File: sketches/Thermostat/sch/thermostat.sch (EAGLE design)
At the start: 11 parts, among them CN1 DHT22, CN2 OLED, SW1 BTN_UP, SW2 BTN_DOWN, SW3 BTN_CTRL, U1 MOTEINO

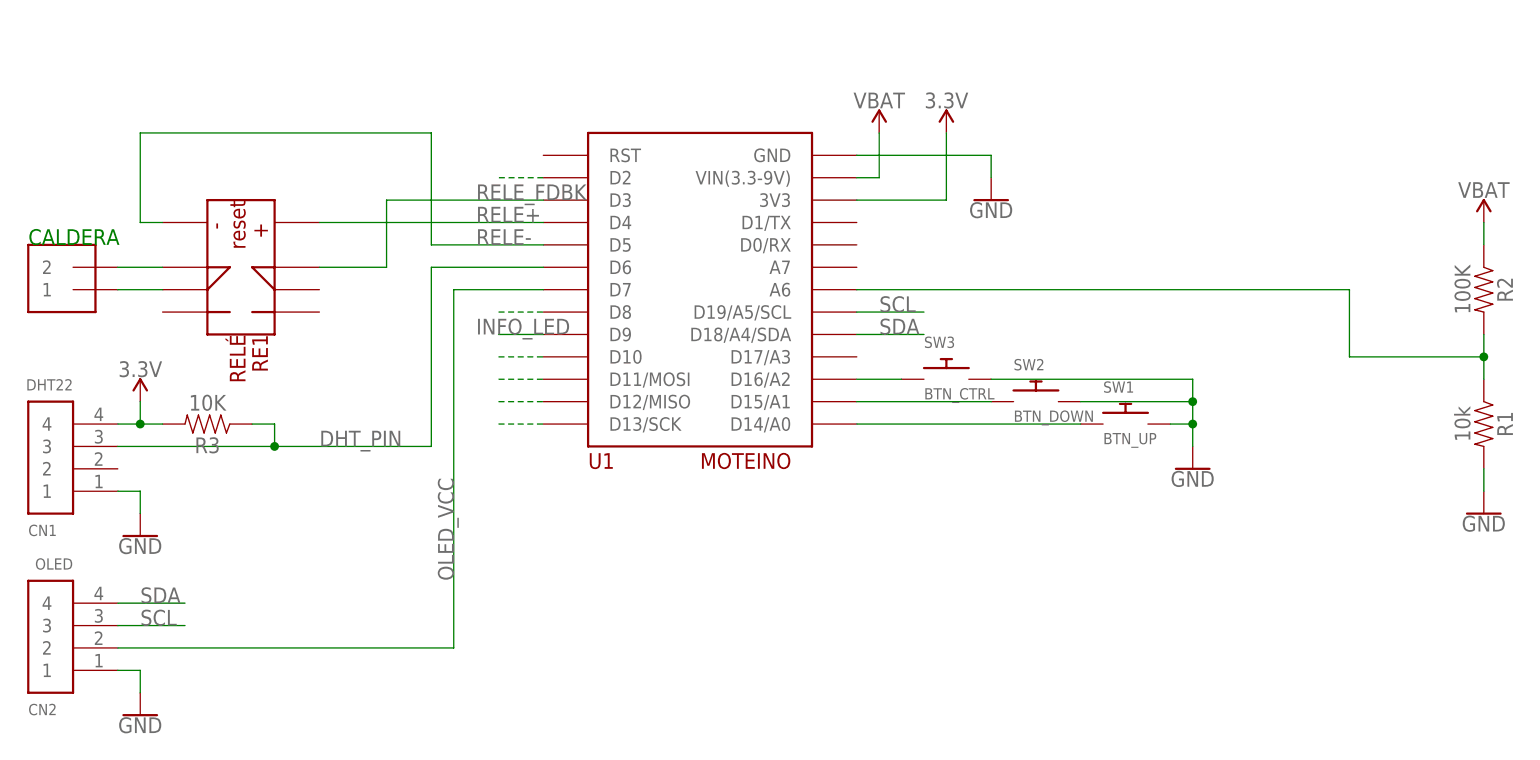
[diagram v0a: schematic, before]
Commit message: [Thermostat] Schematic updated as it is built in real life. v1
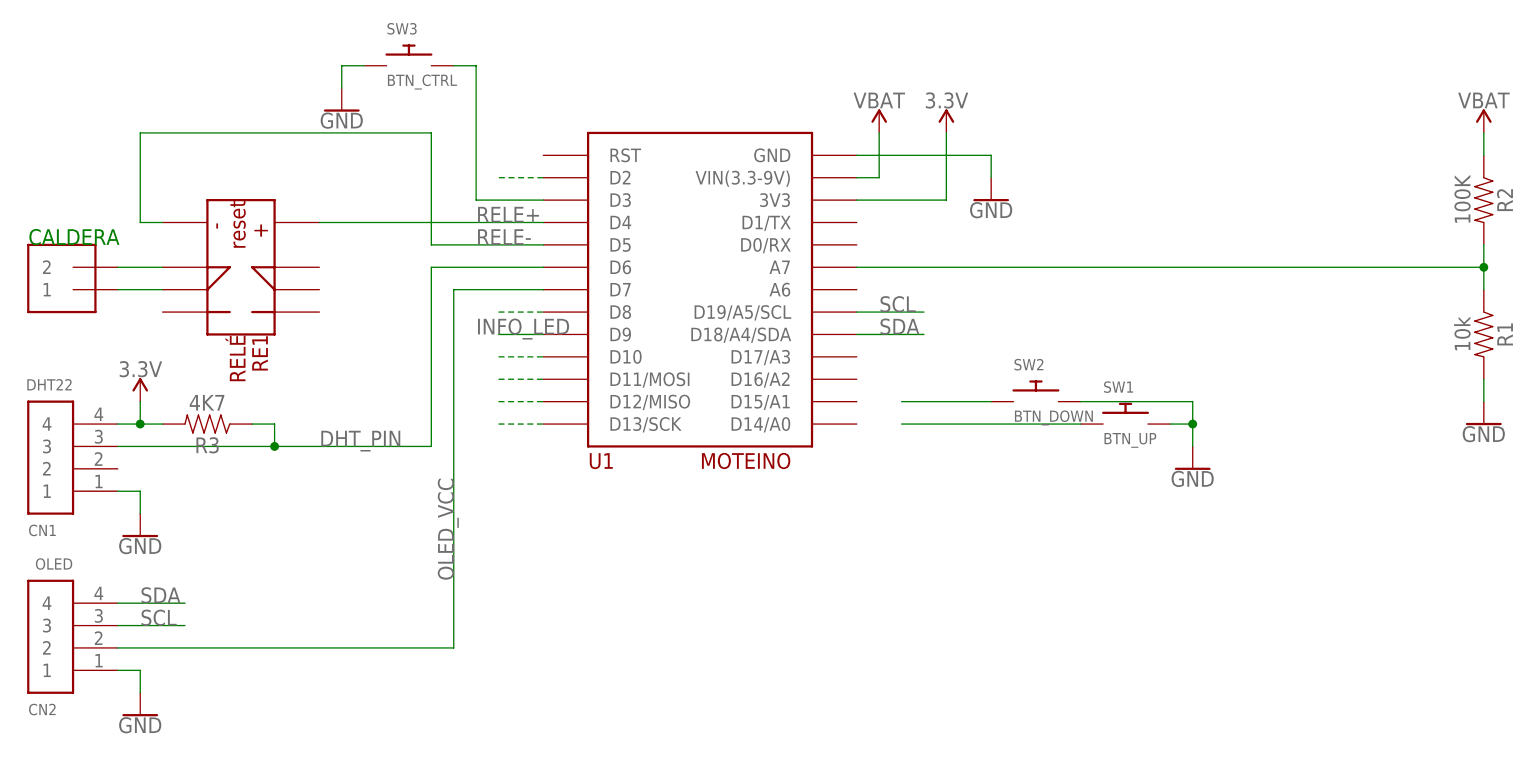
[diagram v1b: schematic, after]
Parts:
- R3: value 10K -> 4K7
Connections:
- removed net RELE_FDBK: RE1.P$8, U1.D3
- net GND: now also SW3.P$1; no longer SW3.P$2
- net N$1: now also SW3.P$2, U1.D3; no longer SW3.P$1, U1.D16/A2
- net N$3: now also U1.A7; no longer U1.A6
- net N$4: no longer U1.D15/A1
- net N$7: no longer U1.D14/A0
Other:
- moved on the sheet: R1, R2, SW3
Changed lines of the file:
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@@
 <part name="SW3" library="adafruit" deviceset="SWITCH_PUSHBUTTON" device="EVQ-PE" value="BTN_CTRL"/>
 <part name="GND6" library="SparkFun-PowerSymbols" deviceset="GND" device=""/>
-<part name="R3" library="SparkFun-Resistors" deviceset="RESISTOR" device="AXIAL-0.3" value="10K"/>
+<part name="R3" library="SparkFun-Resistors" deviceset="RESISTOR" device="AXIAL-0.3" value="4K7"/>
+<part name="GND2" library="SparkFun-PowerSymbols" deviceset="GND" device=""/>
 </parts>
 <sheets>
@@
 </plain>
 <instances>
-<instance part="R1" gate="G$1" x="132.08" y="7.62" rot="R270"/>
-<instance part="R2" gate="G$1" x="132.08" y="22.86" rot="R270"/>
-<instance part="GND1" gate="1" x="132.08" y="-2.54"/>
+<instance part="R1" gate="G$1" x="132.08" y="17.78" rot="R270"/>
+<instance part="R2" gate="G$1" x="132.08" y="33.02" rot="R270"/>
+<instance part="GND1" gate="1" x="132.08" y="7.62"/>
 <instance part="U1" gate="G$1" x="30.48" y="5.08"/>
 <instance part="SW2" gate="G$1" x="81.28" y="10.16"/>
@@
 <instance part="SUPPLY4" gate="G$1" x="63.5" y="40.64"/>
 <instance part="GND5" gate="1" x="76.2" y="33.02"/>
-<instance part="SUPPLY1" gate="G$1" x="132.08" y="30.48"/>
+<instance part="SUPPLY1" gate="G$1" x="132.08" y="40.64"/>
 <instance part="SW1" gate="G$1" x="91.44" y="7.62"/>
-<instance part="SW3" gate="G$1" x="71.12" y="12.7"/>
+<instance part="SW3" gate="G$1" x="10.16" y="48.26"/>
 <instance part="GND6" gate="1" x="99.06" y="2.54"/>
 <instance part="R3" gate="G$1" x="-12.7" y="7.62" rot="R180"/>
+<instance part="GND2" gate="1" x="2.54" y="43.18"/>
 </instances>
 <busses>
@@
 <segment>
 <pinref part="R1" gate="G$1" pin="2"/>
-<wire x1="132.08" y1="2.54" x2="132.08" y2="0" width="0.1524" layer="91"/>
+<wire x1="132.08" y1="12.7" x2="132.08" y2="10.16" width="0.1524" layer="91"/>
 <pinref part="GND1" gate="1" pin="GND"/>
 </segment>
@@
 </segment>
 <segment>
-<pinref part="SW3" gate="G$1" pin="P$2"/>
-<wire x1="76.2" y1="12.7" x2="99.06" y2="12.7" width="0.1524" layer="91"/>
-<wire x1="99.06" y1="12.7" x2="99.06" y2="10.16" width="0.1524" layer="91"/>
 <pinref part="SW2" gate="G$1" pin="P$2"/>
 <wire x1="99.06" y1="10.16" x2="99.06" y2="7.62" width="0.1524" layer="91"/>
 <wire x1="99.06" y1="7.62" x2="99.06" y2="5.08" width="0.1524" layer="91"/>
 <wire x1="86.36" y1="10.16" x2="99.06" y2="10.16" width="0.1524" layer="91"/>
-<junction x="99.06" y="10.16"/>
 <pinref part="SW1" gate="G$1" pin="P$2"/>
 <wire x1="96.52" y1="7.62" x2="99.06" y2="7.62" width="0.1524" layer="91"/>
@@
 <pinref part="GND6" gate="1" pin="GND"/>
 </segment>
+<segment>
+<pinref part="GND2" gate="1" pin="GND"/>
+<wire x1="2.54" y1="45.72" x2="2.54" y2="48.26" width="0.1524" layer="91"/>
+<pinref part="SW3" gate="G$1" pin="P$1"/>
+<wire x1="2.54" y1="48.26" x2="5.08" y2="48.26" width="0.1524" layer="91"/>
+</segment>
 </net>
 <net name="VCC" class="0">
@@
 <segment>
 <pinref part="R2" gate="G$1" pin="1"/>
-<wire x1="132.08" y1="27.94" x2="132.08" y2="30.48" width="0.1524" layer="91"/>
+<wire x1="132.08" y1="38.1" x2="132.08" y2="40.64" width="0.1524" layer="91"/>
 <pinref part="SUPPLY1" gate="G$1" pin="VCC"/>
 </segment>
@@
 <pinref part="R2" gate="G$1" pin="2"/>
 <pinref part="R1" gate="G$1" pin="1"/>
-<wire x1="132.08" y1="12.7" x2="132.08" y2="15.24" width="0.1524" layer="91"/>
-<pinref part="U1" gate="G$1" pin="A6"/>
-<wire x1="132.08" y1="15.24" x2="132.08" y2="17.78" width="0.1524" layer="91"/>
-<wire x1="60.96" y1="22.86" x2="116.84" y2="22.86" width="0.1524" layer="91"/>
-<wire x1="116.84" y1="22.86" x2="116.84" y2="15.24" width="0.1524" layer="91"/>
-<wire x1="116.84" y1="15.24" x2="132.08" y2="15.24" width="0.1524" layer="91"/>
-<junction x="132.08" y="15.24"/>
+<wire x1="132.08" y1="22.86" x2="132.08" y2="25.4" width="0.1524" layer="91"/>
+<wire x1="132.08" y1="25.4" x2="132.08" y2="27.94" width="0.1524" layer="91"/>
+<junction x="132.08" y="25.4"/>
+<pinref part="U1" gate="G$1" pin="A7"/>
+<wire x1="60.96" y1="25.4" x2="132.08" y2="25.4" width="0.1524" layer="91"/>
 </segment>
 </net>
@@
 </segment>
 </net>
-<net name="RELE_FDBK" class="0">
-<segment>
-<pinref part="RE1" gate="G$1" pin="P$8"/>
-<wire x1="0" y1="25.4" x2="7.62" y2="25.4" width="0.1524" layer="91"/>
-<wire x1="7.62" y1="25.4" x2="7.62" y2="33.02" width="0.1524" layer="91"/>
+<net name="N$1" class="0">
+<segment>
+<pinref part="SW3" gate="G$1" pin="P$2"/>
+<wire x1="15.24" y1="48.26" x2="17.78" y2="48.26" width="0.1524" layer="91"/>
+<wire x1="17.78" y1="48.26" x2="17.78" y2="33.02" width="0.1524" layer="91"/>
 <pinref part="U1" gate="G$1" pin="D3"/>
-<wire x1="7.62" y1="33.02" x2="25.4" y2="33.02" width="0.1524" layer="91"/>
-<label x="17.78" y="33.02" size="1.778" layer="95"/>
-</segment>
-</net>
-<net name="N$1" class="0">
-<segment>
-<pinref part="U1" gate="G$1" pin="D16/A2"/>
-<pinref part="SW3" gate="G$1" pin="P$1"/>
-<wire x1="60.96" y1="12.7" x2="66.04" y2="12.7" width="0.1524" layer="91"/>
+<wire x1="17.78" y1="33.02" x2="25.4" y2="33.02" width="0.1524" layer="91"/>
 </segment>
 </net>
 <net name="N$4" class="0">
 <segment>
-<pinref part="U1" gate="G$1" pin="D15/A1"/>
 <pinref part="SW2" gate="G$1" pin="P$1"/>
-<wire x1="60.96" y1="10.16" x2="76.2" y2="10.16" width="0.1524" layer="91"/>
+<wire x1="66.04" y1="10.16" x2="76.2" y2="10.16" width="0.1524" layer="91"/>
 </segment>
 </net>
 <net name="N$7" class="0">
 <segment>
-<pinref part="U1" gate="G$1" pin="D14/A0"/>
 <pinref part="SW1" gate="G$1" pin="P$1"/>
-<wire x1="60.96" y1="7.62" x2="86.36" y2="7.62" width="0.1524" layer="91"/>
-</segment>
-</net>
+<wire x1="66.04" y1="7.62" x2="86.36" y2="7.62" width="0.1524" layer="91"/>
+</segment>
+</net>

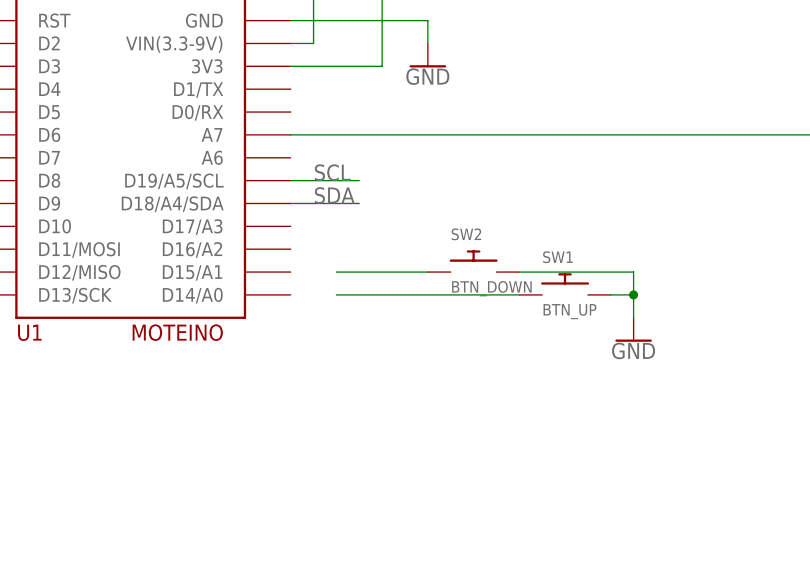
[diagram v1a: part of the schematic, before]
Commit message: [Thermostat] ButtonUp & Down implemented. RTC removed. TODO. Relay feedback / adjust DHT22 reading routine.
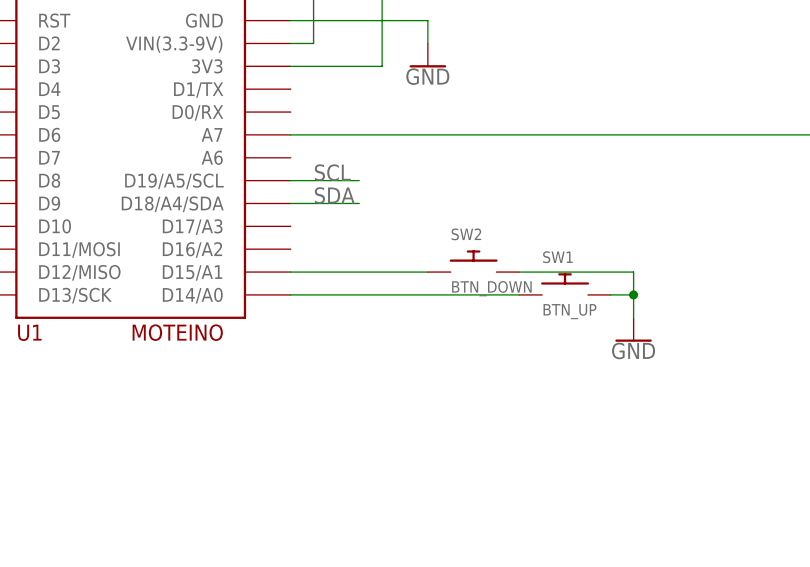
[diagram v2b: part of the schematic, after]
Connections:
- net N$4: now also U1.D15/A1
- net N$7: now also U1.D14/A0
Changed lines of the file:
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@@
 <segment>
 <pinref part="SW2" gate="G$1" pin="P$1"/>
-<wire x1="66.04" y1="10.16" x2="76.2" y2="10.16" width="0.1524" layer="91"/>
+<wire x1="60.96" y1="10.16" x2="76.2" y2="10.16" width="0.1524" layer="91"/>
+<pinref part="U1" gate="G$1" pin="D15/A1"/>
 </segment>
 </net>
@@
 <segment>
 <pinref part="SW1" gate="G$1" pin="P$1"/>
-<wire x1="66.04" y1="7.62" x2="86.36" y2="7.62" width="0.1524" layer="91"/>
+<wire x1="60.96" y1="7.62" x2="86.36" y2="7.62" width="0.1524" layer="91"/>
+<pinref part="U1" gate="G$1" pin="D14/A0"/>
 </segment>
 </net>

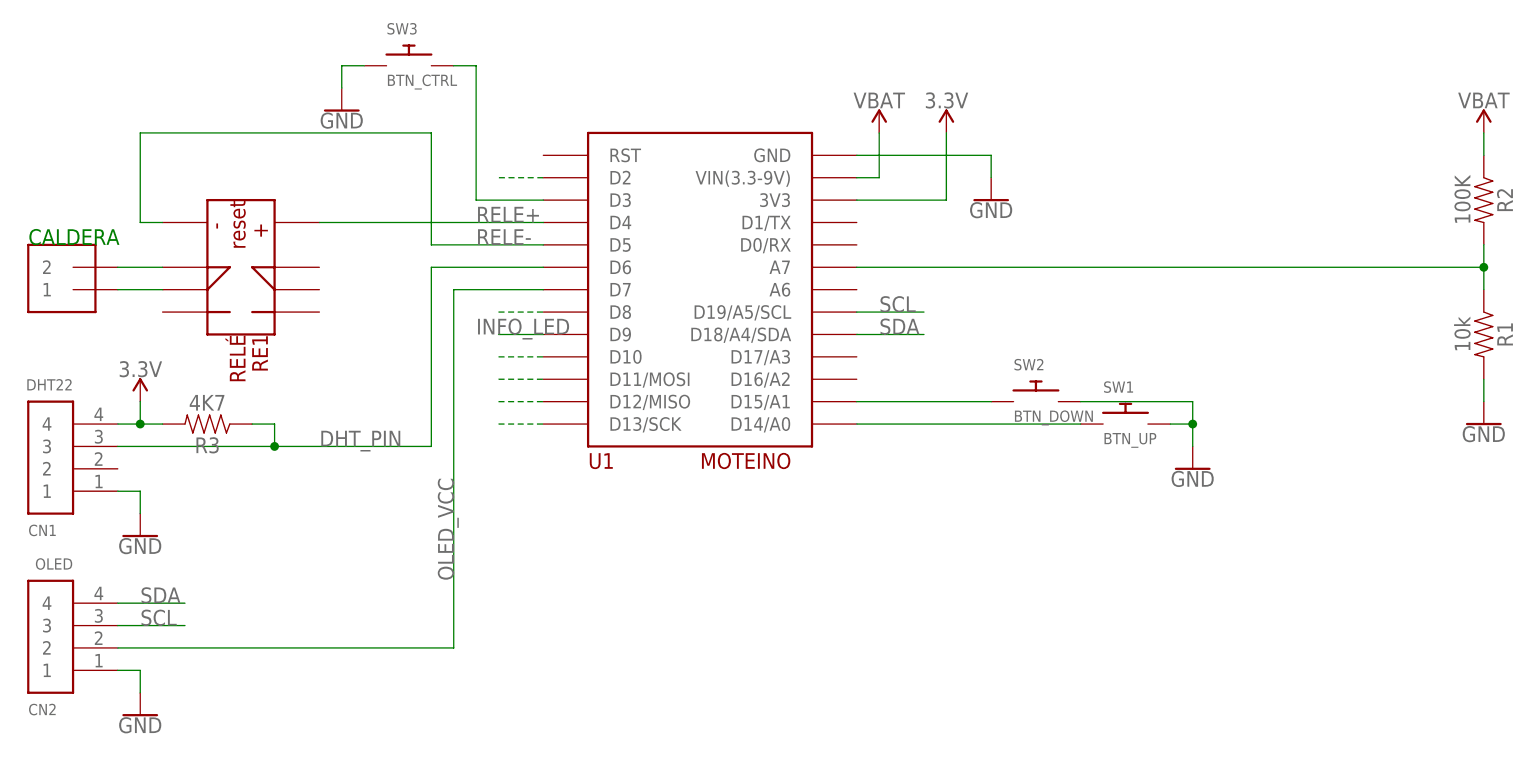
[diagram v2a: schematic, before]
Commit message: [Thermostat] Relay feedback implemented.
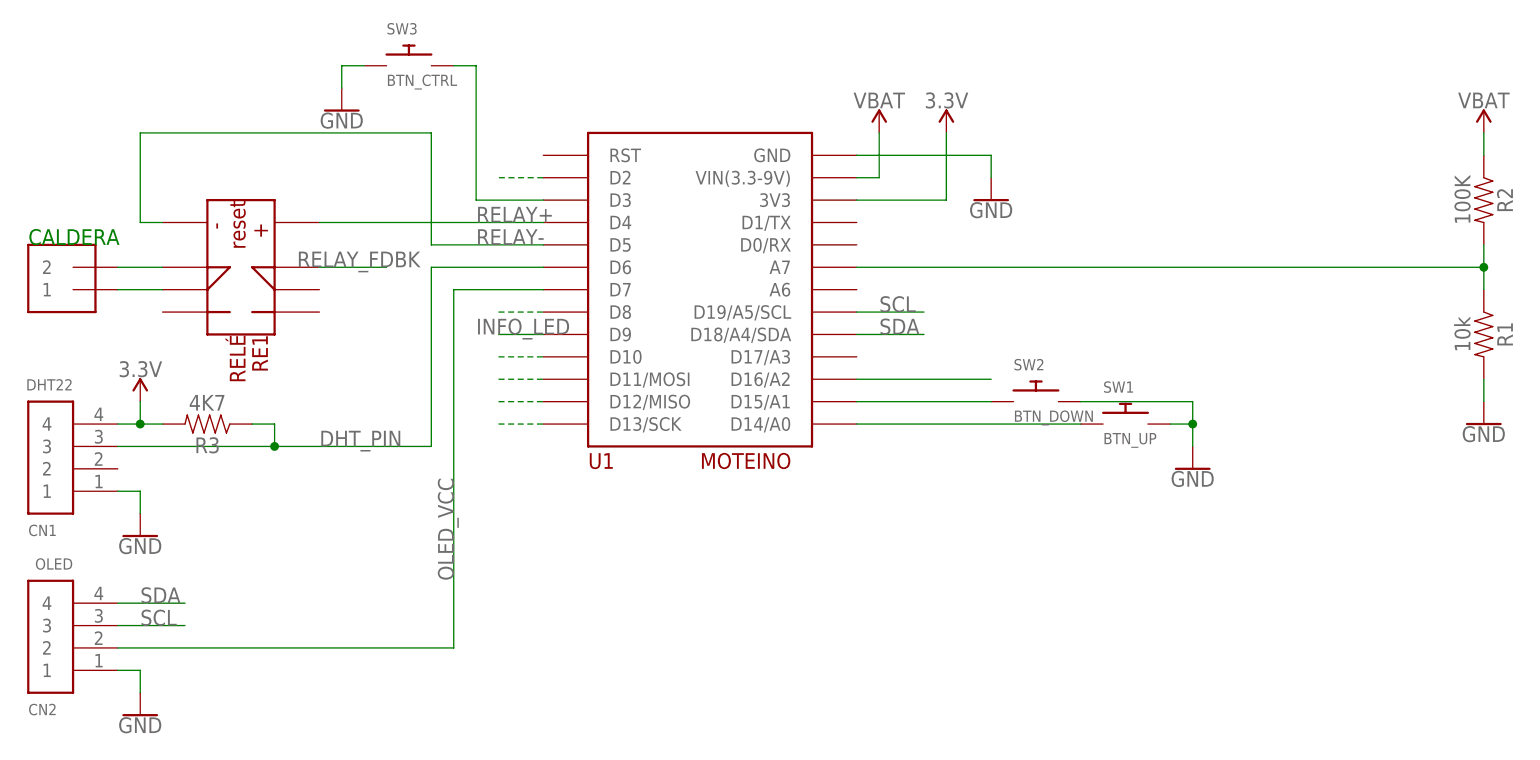
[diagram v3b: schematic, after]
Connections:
- net RELE+ renamed RELAY+
- net RELE- renamed RELAY-
- new net RELAY_FDBK: RE1.P$8, U1.D16/A2
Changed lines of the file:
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@@
 </segment>
 </net>
-<net name="RELE+" class="0">
+<net name="RELAY+" class="0">
 <segment>
 <pinref part="U1" gate="G$1" pin="D4"/>
@@
 </segment>
 </net>
-<net name="RELE-" class="0">
+<net name="RELAY-" class="0">
 <segment>
 <pinref part="U1" gate="G$1" pin="D5"/>
@@
 </segment>
 </net>
+<net name="RELAY_FDBK" class="0">
+<segment>
+<pinref part="RE1" gate="G$1" pin="P$8"/>
+<wire x1="0" y1="25.4" x2="7.62" y2="25.4" width="0.1524" layer="91"/>
+<label x="-2.54" y="25.4" size="1.778" layer="95"/>
+</segment>
+<segment>
+<pinref part="U1" gate="G$1" pin="D16/A2"/>
+<wire x1="60.96" y1="12.7" x2="76.2" y2="12.7" width="0.1524" layer="91"/>
+</segment>
+</net>
